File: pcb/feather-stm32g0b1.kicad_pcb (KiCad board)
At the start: 4 copper layers, 50.8 x 22.9 mm, 48 parts, among them CN1 STDC14, CN2 SM04B-SRSS-TB (LF)(SN), CN3 ZX-PH2.0-WT2P, CN4 SM04B-SRSS-TB (LF)(SN), J1 Conn_01x12, J2 Conn_01x16, J3 GT-USB-7010ASV, Q1 DMG3415U-7, SW1 SW_Push, U1 STM32G0B1CBT6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

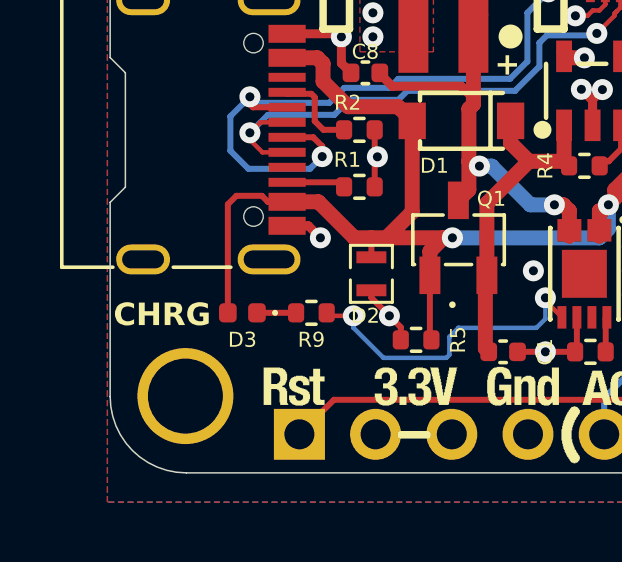
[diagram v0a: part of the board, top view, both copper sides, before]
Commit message: Renamed kicad project
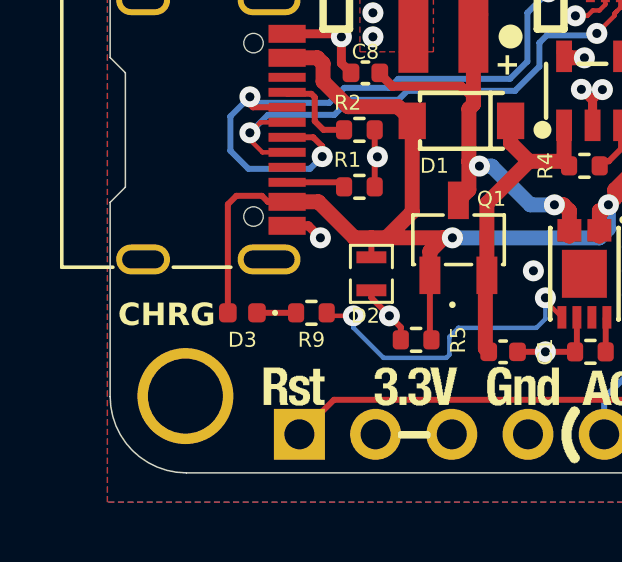
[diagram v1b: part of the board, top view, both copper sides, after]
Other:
- board text added: "Feather STM32G0B1 Rev. B Community Feather"
- board text removed: "Feather STM32G0B1 Rev. A Community Feather"
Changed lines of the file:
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@@
 	)
 	(gr_text "CHRG"
-		(at 100.2 97.5 0)
+		(at 100.35 97.5 0)
 		(layer "F.SilkS")
 		(effects
@@
 		)
 	)
-	(gr_text "Feather STM32G0B1 Rev. A\nCommunity Feather"
+	(gr_text "Feather STM32G0B1 Rev. B\nCommunity Feather"
 		(at 147.8 89.1 0)
 		(layer "B.SilkS")

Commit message: Lots more work on RevB schematics and pcb
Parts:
- added R16: 5K1, Resistor_SMD:R_0402_1005Metric, F.Cu at (122.6, 89.3)
- added R17: 5K1, Resistor_SMD:R_0402_1005Metric, F.Cu at (126.1, 84.3)
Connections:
- U1 pad 11: ANALOG0 -> ANALOG4
- U1 pad 12: ANALOG1 -> ANALOG5
- U1 pad 15: ANALOG4 -> ANALOG0
- U1 pad 16: ANALOG5 -> ANALOG1
- U1 pad 17: unconnected-(U1-PA6-Pad17) -> DIGITAL6
- U1 pad 19: unconnected-(U1-PB0-Pad19) -> DIGITAL5
- U1 pad 27: DIGITAL5 -> unconnected-(U1-PB15-Pad27)
- U1 pad 28: DIGITAL6 -> unconnected-(U1-PA8-Pad28)
- U1 pad 37: DIGITAL9 -> unconnected-(U1-PA15-Pad37)
- U1 pad 38: DIGITAL10 -> unconnected-(U1-PD0-Pad38)
- U1 pad 39: DIGITAL11 -> unconnected-(U1-PD1-Pad39)
- U1 pad 40: DIGITAL12 -> unconnected-(U1-PD2-Pad40)
- U1 pad 41: DIGITAL13 -> unconnected-(U1-PD3-Pad41)
- U1 pad 44: unconnected-(U1-PB5-Pad44) -> DIGITAL9
- U1 pad 45: unconnected-(U1-PB6-Pad45) -> DIGITAL10
- U1 pad 46: unconnected-(U1-PB7-Pad46) -> DIGITAL11
- U1 pad 47: unconnected-(U1-PB8-Pad47) -> DIGITAL12
- U1 pad 48: unconnected-(U1-PB9-Pad48) -> DIGITAL13
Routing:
- net +3V3: track 81.6 -> 94.3 mm, vias 7 -> 8
- net ANALOG0: track 14.5 -> 21.9 mm
- net ANALOG1: track 12.1 -> 19.0 mm, vias 0 -> 2
- net I2C3_SCL: track 32.7 -> 38.2 mm, vias 4 -> 3
- net ANALOG4: track 12.9 -> 7.93 mm, vias 1 -> 0
- net NRST: track 49.3 -> 54.0 mm
- net I2C3_SDA: track 34.9 -> 39.5 mm
- net DIGITAL6: track 18.7 -> 22.7 mm
- net DIGITAL9: track 11.4 -> 14.9 mm
- net DIGITAL10: track 9.99 -> 13.4 mm
- net DIGITAL11: track 8.52 -> 11.7 mm
- net DIGITAL12: track 6.98 -> 10.1 mm
- net DIGITAL5: track 20.2 -> 23.0 mm
- net DIGITAL13: track 6.55 -> 8.87 mm
- net ANALOG3: track 14.2 -> 15.1 mm
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
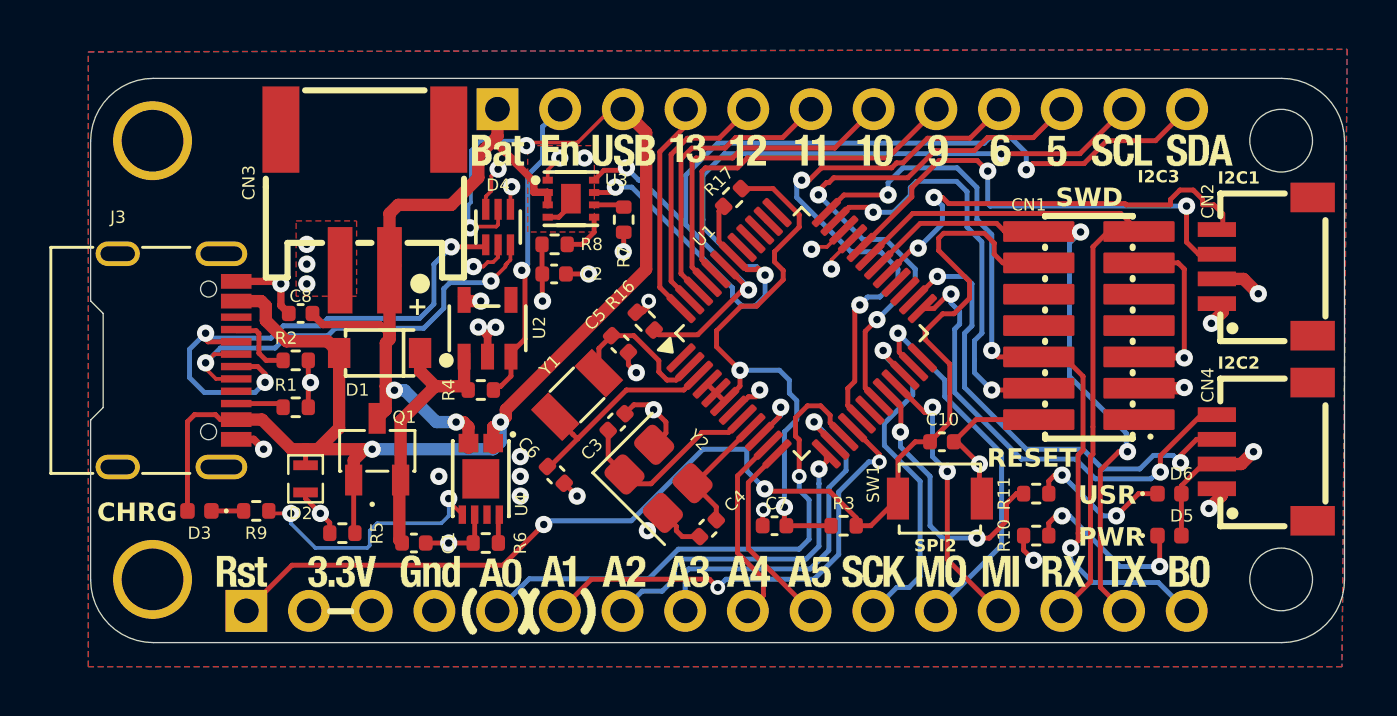
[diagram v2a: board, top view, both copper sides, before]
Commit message: Switched battery and QWIIC connectors to black ones, and fixed their positioning to not obstruct bolt heads when M2.5 cylindrical bolts are used to mount the board
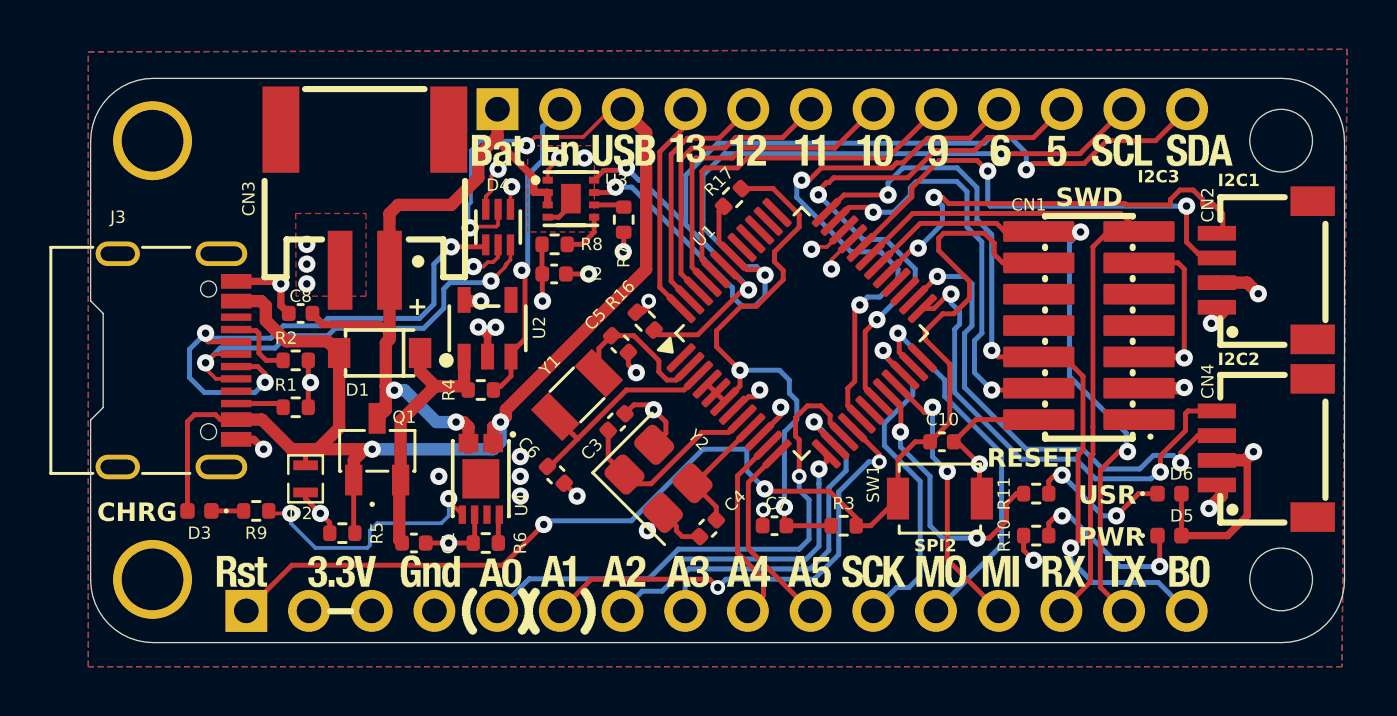
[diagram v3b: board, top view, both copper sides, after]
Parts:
- CN3: footprint prop-devboard:CONN-SMD_ZX-PH2.0-WT2P -> prop-devboard:CONN-SMD_PH-2AWT
- moved CN2 0.15 mm to (147.7, 87.2)
- moved CN4 0.15 mm to (147.7, 94.5)
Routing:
- net +3V3: track 94.3 -> 98.0 mm
- net GND: track 49.1 -> 47.6 mm
- net VBAT: track 30.3 -> 29.1 mm
- net I2C2_SCL: track 19.2 -> 20.2 mm
